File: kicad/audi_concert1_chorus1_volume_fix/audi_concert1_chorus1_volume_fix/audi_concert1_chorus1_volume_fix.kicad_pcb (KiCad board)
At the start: 2 copper layers, 14 parts, among them U2 AP1117-33

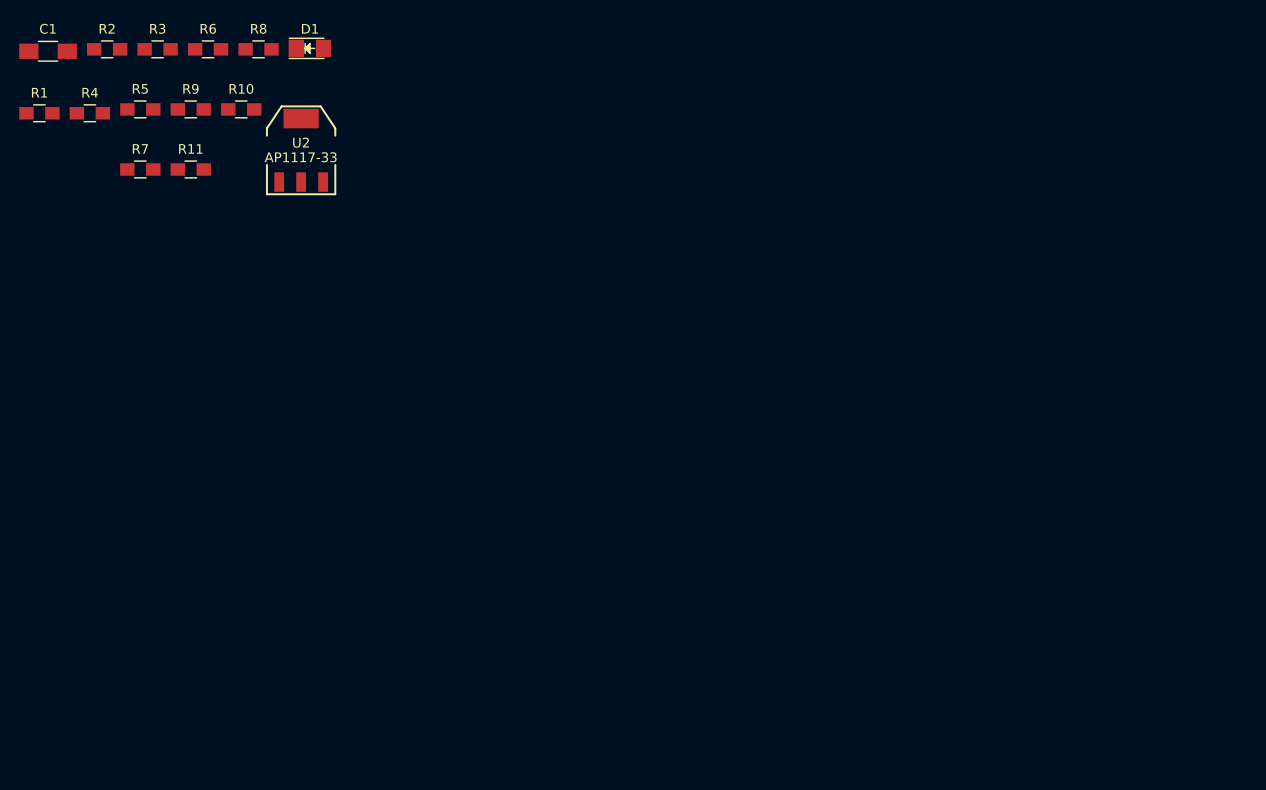
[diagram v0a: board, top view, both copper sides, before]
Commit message: moved to separed repository audi_concert1_chorus1_volume_fix
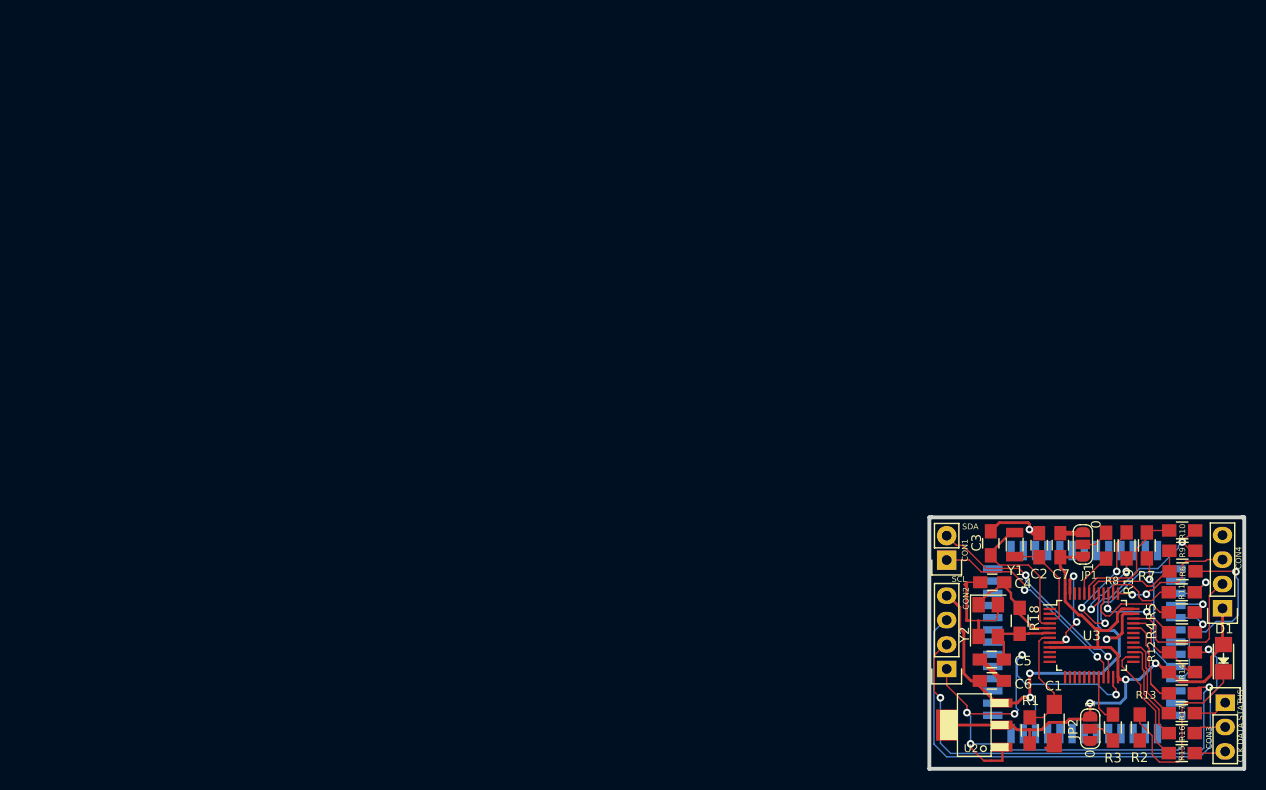
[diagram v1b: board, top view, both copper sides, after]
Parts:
- added C2: 22p, Capacitors_SMD.pretty:C_0805_HandSoldering, F.Cu at (175.3, 96.6)
- added C3: 22p, Capacitors_SMD.pretty:C_0805_HandSoldering, F.Cu at (170.2, 96.4)
- added C4: 22p, Capacitors_SMD.pretty:C_0805_HandSoldering, F.Cu at (170.4, 100.5)
- added C5: 22p, Capacitors_SMD.pretty:C_0805_HandSoldering, F.Cu at (170.3, 108.5)
- added C6: 100n, Capacitors_SMD.pretty:C_0805_HandSoldering, F.Cu at (170.3, 110.7)
- added C7: 100n, Capacitors_SMD.pretty:C_0805_HandSoldering, F.Cu at (177.5, 96.6)
- added CON1: I2C_to_TDA, Pin_Headers.pretty:Pin_Header_Straight_1x02, F.Cu at (165.6, 98.2)
- added CON2: USB, Pin_Headers.pretty:Pin_Header_Straight_1x04, F.Cu at (165.6, 109.5)
- added CON3: SPI_TO_PANEL, Pin_Headers.pretty:Pin_Header_Straight_1x03, F.Cu at (194.6, 113.0)
- added CON4: JLINK, Pin_Headers.pretty:Pin_Header_Straight_1x04, F.Cu at (194.3, 103.2)
- added JP1: SolderJumper_3_Open, Jumper:SolderJumper-3_P1.3mm_Open_RoundedPad1.0x1.5mm_NumberLabels, F.Cu at (179.8, 96.5)
- added JP2: SolderJumper_3_Open, Jumper:SolderJumper-3_P1.3mm_Open_RoundedPad1.0x1.5mm_NumberLabels, F.Cu at (180.6, 115.7)
- added R12: 20, Resistors_SMD.pretty:R_0805_HandSoldering, F.Cu at (190.1, 107.8)
- added R13: 20, Resistors_SMD.pretty:R_0805_HandSoldering, F.Cu at (190.1, 112.0)
- added R14: 1k5, Resistors_SMD.pretty:R_0805_HandSoldering, F.Cu at (190.1, 109.8)
- added R15: 1k, Resistors_SMD.pretty:R_0805_HandSoldering, F.Cu at (190.1, 118.3)
- added R16: 1k, Resistors_SMD.pretty:R_0805_HandSoldering, F.Cu at (190.1, 116.2)
- added R17: 1k, Resistors_SMD.pretty:R_0805_HandSoldering, F.Cu at (190.1, 114.1)
- added R18: 1M, Resistors_SMD.pretty:R_0805_HandSoldering, F.Cu at (173.2, 104.5)
- added R19: 1k, Resistors_SMD.pretty:R_0805_HandSoldering, F.Cu at (184.4, 96.6)
- added U1: 68HC05_PLCC, modules:PLCC-52_mirrored, F.Cu at (180.0, 106.7)
- added U3: STM32F103C8Tx, Housings_QFP:LQFP-48_7x7mm_Pitch0.5mm, F.Cu at (180.7, 106.0)
- added Y1: Crystal_GND24, Crystals:Crystal_SMD_3215-2pin_3.2x1.5mm, F.Cu at (172.7, 96.6)
- added Y2: Crystal_GND24, Crystals:Crystal_SMD_5032-4pin_5.0x3.2mm, F.Cu at (170.0, 104.5)
- U2: footprint modules:SOT-223-REGULATOR -> ab2_sot.mod:AB2_SOT223
- moved R2 128.5 mm to (185.7, 115.6), turned to 90 degrees
- moved C1 125.9 mm to (176.8, 115.2), turned to 270 degrees
- moved R4 125.8 mm to (190.1, 105.7)
- moved R3 121.9 mm to (182.9, 115.6), turned to 270 degrees
- moved R1 121.4 mm to (174.3, 115.9), turned to 270 degrees
- moved R5 120.3 mm to (190.1, 103.6), turned to 180 degrees
- moved R6 115.0 mm to (190.2, 99.3)
- moved D1 114.3 mm to (194.4, 108.4), turned to 90 degrees
- moved R9 112.9 mm to (190.2, 97.2), turned to 180 degrees
- moved R11 112.1 mm to (190.1, 101.5)
- moved R7 111.8 mm to (186.5, 96.7), turned to 270 degrees
- moved R10 107.3 mm to (190.1, 95.1)
- moved R8 102.2 mm to (182.2, 96.7), turned to 90 degrees
- moved U2 92.1 mm to (168.5, 115.3), turned to 90 degrees
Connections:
- R11 pad 1: (no net) -> Net-(R11-Pad1)
- R11 pad 2: (no net) -> /STATUS_FROM_MCU
- R3 pad 1: (no net) -> Net-(R3-Pad1)
- R3 pad 2: (no net) -> /BOOT1
- R4 pad 1: (no net) -> Net-(R4-Pad1)
- R4 pad 2: (no net) -> /CLOCK_FROM_MCU
- R5 pad 1: (no net) -> /DATA_FROM_MCU
- R5 pad 2: (no net) -> Net-(R5-Pad2)
- R6 pad 2: (no net) -> /SCL_FROM_MOTO
- R7 pad 2: (no net) -> /SDA_FROM_MOTO
- R8 pad 1: (no net) -> Net-(R8-Pad1)
- R8 pad 2: (no net) -> /BOOT0
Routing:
- net GND: track 0.00 -> 105.2 mm, vias 0 -> 10
- net 3V3: track 0.00 -> 75.9 mm, vias 0 -> 3
- net 5V: track 0.00 -> 56.5 mm, vias 0 -> 3
- net Net-(CON2-Pad3): track 0.00 -> 55.6 mm, vias 0 -> 1
- net Net-(CON2-Pad2): track 0.00 -> 47.6 mm, vias 0 -> 2
- net /SDA_TO_TDA: track 0.00 -> 24.5 mm, vias 0 -> 2
- net /RESET_KA: track 0.00 -> 24.4 mm, vias 0 -> 3
- net /SCL_TO_TDA: track 0.00 -> 22.6 mm, vias 0 -> 2
- net Net-(D1-Pad1): track 0.00 -> 20.1 mm
- net /SCL_FROM_MOTO: track 0.00 -> 20.1 mm, vias 0 -> 1
- net /SWDIO: track 0.00 -> 16.3 mm
- net /OSC32OUT: track 0.00 -> 15.5 mm
- net Net-(R10-Pad1): track 0.00 -> 14.0 mm
- net /SDA_FROM_MOTO: track 0.00 -> 13.5 mm, vias 0 -> 1
- net /SWDCLK: track 0.00 -> 13.2 mm, vias 0 -> 2
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- added copper zone on B.Cu, net GND
- added copper zone on F.Cu, net GND
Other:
- board outline added: 32.8 x 26.2 mm
- net class 3v3 added: clearance 0.2, trace_width 0.3, via_dia 0.8, via_drill 0.4
- net class 5V added: clearance 0.2, trace_width 0.3, via_dia 0.8, via_drill 0.4
- net class Default: trace_width 0.25 -> 0.15
- net class GND added: clearance 0.2, trace_width 0.3, via_dia 0.8, via_drill 0.4
- rule trace_min: 0.2 -> 0.1
- board text added: "CLK DATA STATUS"
- board text added: "SCL"
- board text added: "SDA"
